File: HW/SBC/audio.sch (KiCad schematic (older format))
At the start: 13 parts, among them U13 LM386, U14 AY-3-8912

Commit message: Connected most hierarchical labels between the sheets. Added a connector to AY IO port.
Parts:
- added J6: AY-IO, Connect:IDC_Header_Straight_14pins, symbol CONN_02X07
- C16, C18, C19, C20: footprint (none) -> Capacitors_ThroughHole:C_Disc_D3.8mm_W2.6mm_P2.50mm
- C21: footprint (none) -> Capacitors_ThroughHole:CP_Radial_D6.3mm_P2.50mm
- LS1: footprint (none) -> Connect:PJ311_3.5mm_Jack
- R1, R2, R3, R4, R5: footprint (none) -> Resistors_ThroughHole:R_Axial_DIN0411_L9.9mm_D3.6mm_P12.70mm_Horizontal
- U13: footprint (none) -> Housings_DIP:DIP-8_W7.62mm_Socket
- U14: footprint (none) -> Housings_DIP:DIP-28_W15.24mm_Socket
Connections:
- net GND: now also J6.1 (P1), J6.2 (P2)
- net IO_A0: now also J6.5 (P5)
- net IO_A1: now also J6.6 (P6)
- net IO_A2: now also J6.7 (P7)
- net IO_A3: now also J6.8 (P8)
- net IO_A4: now also J6.9 (P9)
- net IO_A5: now also J6.10 (P10)
- net IO_A6: now also J6.11 (P11)
- net IO_A7: now also J6.12 (P12)
- net VCC: now also U14.19 (BC2), J6.13 (P13), J6.14 (P14)
- net CLK: now reaches U14.15 (CLK)
- net ~RES: now reaches U14.16 (~RESET)
- net V2CA1: now reaches U14.18 (BDir)
- net V2CA2: now reaches U14.20 (BC1)
- no-connect marks 4 -> 7
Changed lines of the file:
@@
 F 0 "U14" H 4775 4375 60  0000 C CNN
 F 1 "AY-3-8912" V 4975 3675 60  0000 C CNN
-F 2 "" H 4850 3900 60  0001 C CNN
+F 2 "Housings_DIP:DIP-28_W15.24mm_Socket" H 4850 3900 60  0001 C CNN
 F 3 "" H 4850 3900 60  0001 C CNN
 	1    4950 3675
@@
 F 0 "U13" H 3400 1875 50  0000 L CNN
 F 1 "LM386" H 3400 1775 50  0000 L CNN
-F 2 "" H 3450 1675 50  0001 C CNN
+F 2 "Housings_DIP:DIP-8_W7.62mm_Socket" H 3450 1675 50  0001 C CNN
 F 3 "" H 3550 1775 50  0001 C CNN
 	1    3350 1575
@@
 F 0 "LS1" H 4925 1800 50  0000 R CNN
 F 1 "Speaker" H 4925 1725 50  0000 R CNN
-F 2 "" H 4875 1375 50  0001 C CNN
+F 2 "Connect:PJ311_3.5mm_Jack" H 4875 1375 50  0001 C CNN
 F 3 "" H 4865 1525 50  0001 C CNN
 	1    4875 1575
@@
 F 0 "C19" H 3025 3825 50  0000 L CNN
 F 1 "10nF" H 2675 3825 50  0000 L CNN
-F 2 "" H 2950 3825 50  0001 C CNN
+F 2 "Capacitors_ThroughHole:C_Disc_D3.8mm_W2.6mm_P2.50mm" H 2950 3825 50  0001 C CNN
 F 3 "" H 2950 3825 50  0001 C CNN
 	1    2950 3825
@@
 F 0 "C16" V 2900 3450 50  0000 L CNN
 F 1 "2.2nF" V 2575 3425 50  0000 L CNN
-F 2 "" H 2750 3475 50  0001 C CNN
+F 2 "Capacitors_ThroughHole:C_Disc_D3.8mm_W2.6mm_P2.50mm" H 2750 3475 50  0001 C CNN
 F 3 "" H 2750 3475 50  0001 C CNN
 	1    2750 3475
@@
 F 0 "C18" V 2675 1075 50  0000 L CNN
 F 1 "10uF" V 2925 1025 50  0000 L CNN
-F 2 "" H 2800 1125 50  0001 C CNN
+F 2 "Capacitors_ThroughHole:C_Disc_D3.8mm_W2.6mm_P2.50mm" H 2800 1125 50  0001 C CNN
 F 3 "" H 2800 1125 50  0001 C CNN
 	1    2800 1125
@@
 U 1 1 59307F57
 P 3900 1775
-F 0 "C20" H 3910 1845 50  0000 L CNN
+F 0 "C20" H 3725 1700 50  0000 L CNN
 F 1 "47nF" H 3910 1695 50  0000 L CNN
-F 2 "" H 3900 1775 50  0001 C CNN
+F 2 "Capacitors_ThroughHole:C_Disc_D3.8mm_W2.6mm_P2.50mm" H 3900 1775 50  0001 C CNN
 F 3 "" H 3900 1775 50  0001 C CNN
 	1    3900 1775
@@
 F 0 "R3" V 3575 3450 50  0000 L CNN
 F 1 "4.7k" V 3400 3450 50  0000 L CNN
-F 2 "" H 3500 3475 50  0001 C CNN
+F 2 "Resistors_ThroughHole:R_Axial_DIN0411_L9.9mm_D3.6mm_P12.70mm_Horizontal" H 3500 3475 50  0001 C CNN
 F 3 "" H 3500 3475 50  0001 C CNN
 	1    3500 3475
@@
 F 0 "R4" H 3755 3845 50  0000 L CNN
 F 1 "1k" H 3755 3785 50  0000 L CNN
-F 2 "" H 3725 3825 50  0001 C CNN
+F 2 "Resistors_ThroughHole:R_Axial_DIN0411_L9.9mm_D3.6mm_P12.70mm_Horizontal" H 3725 3825 50  0001 C CNN
 F 3 "" H 3725 3825 50  0001 C CNN
 	1    3725 3825
@@
 F 0 "R5" V 3825 2025 50  0000 L CNN
 F 1 "10" V 3975 2025 50  0000 L CNN
-F 2 "" H 3900 2075 50  0001 C CNN
+F 2 "Resistors_ThroughHole:R_Axial_DIN0411_L9.9mm_D3.6mm_P12.70mm_Horizontal" H 3900 2075 50  0001 C CNN
 F 3 "" H 3900 2075 50  0001 C CNN
 	1    3900 2075
@@
 F 0 "R2" H 3275 3850 50  0000 L CNN
 F 1 "470" H 3275 3775 50  0000 L CNN
-F 2 "" H 3225 3825 50  0001 C CNN
+F 2 "Resistors_ThroughHole:R_Axial_DIN0411_L9.9mm_D3.6mm_P12.70mm_Horizontal" H 3225 3825 50  0001 C CNN
 F 3 "" H 3225 3825 50  0001 C CNN
 	1    3225 3825
@@
 F 0 "R1" V 2625 1650 50  0000 L CNN
 F 1 "22k" V 2775 1625 50  0000 L CNN
-F 2 "" H 2700 1675 50  0001 C CNN
+F 2 "Resistors_ThroughHole:R_Axial_DIN0411_L9.9mm_D3.6mm_P12.70mm_Horizontal" H 2700 1675 50  0001 C CNN
 F 3 "" H 2700 1675 50  0001 C CNN
 	1    2700 1675
@@
 F 0 "C21" V 4400 1525 50  0000 L CNN
 F 1 "220uF 10V" V 4150 1400 50  0000 L CNN
-F 2 "" H 4275 1575 50  0001 C CNN
+F 2 "Capacitors_ThroughHole:CP_Radial_D6.3mm_P2.50mm" H 4275 1575 50  0001 C CNN
 F 3 "" H 4275 1575 50  0001 C CNN
 	1    4275 1575
@@
 NoConn ~ 3350 1275
 $Comp
-L GND #PWR47
+L GND #PWR044
 U 1 1 59309AB4
 P 3250 2500
-F 0 "#PWR47" H 3250 2250 50  0001 C CNN
+F 0 "#PWR044" H 3250 2250 50  0001 C CNN
 F 1 "GND" H 3250 2350 50  0000 C CNN
 F 2 "" H 3250 2500 50  0001 C CNN
@@
 $EndComp
 $Comp
-L GND #PWR45
+L GND #PWR045
 U 1 1 5930A8FE
 P 2525 1125
-F 0 "#PWR45" H 2525 875 50  0001 C CNN
+F 0 "#PWR045" H 2525 875 50  0001 C CNN
 F 1 "GND" H 2525 975 50  0000 C CNN
 F 2 "" H 2525 1125 50  0001 C CNN
@@
 $EndComp
 $Comp
-L GND #PWR44
+L GND #PWR046
 U 1 1 5930AC61
 P 2300 4100
-F 0 "#PWR44" H 2300 3850 50  0001 C CNN
+F 0 "#PWR046" H 2300 3850 50  0001 C CNN
 F 1 "GND" H 2300 3950 50  0000 C CNN
 F 2 "" H 2300 4100 50  0001 C CNN
@@
 NoConn ~ 4450 3075
 $Comp
-L VCC #PWR48
+L VCC #PWR047
 U 1 1 5930B1EC
 P 4950 2725
-F 0 "#PWR48" H 4950 2575 50  0001 C CNN
+F 0 "#PWR047" H 4950 2575 50  0001 C CNN
 F 1 "VCC" H 4950 2875 50  0000 C CNN
 F 2 "" H 4950 2725 50  0001 C CNN
@@
 $EndComp
 $Comp
-L VCC #PWR46
+L VCC #PWR048
 U 1 1 5930B242
 P 3250 1075
-F 0 "#PWR46" H 3250 925 50  0001 C CNN
+F 0 "#PWR048" H 3250 925 50  0001 C CNN
 F 1 "VCC" H 3250 1225 50  0000 C CNN
 F 2 "" H 3250 1075 50  0001 C CNN
@@
 $EndComp
 $Comp
-L GND #PWR49
+L GND #PWR049
 U 1 1 5930BB05
 P 4950 4750
-F 0 "#PWR49" H 4950 4500 50  0001 C CNN
+F 0 "#PWR049" H 4950 4500 50  0001 C CNN
 F 1 "GND" H 4950 4600 50  0000 C CNN
 F 2 "" H 4950 4750 50  0001 C CNN
@@
 	5450 3775 5725 3775
 Wire Bus Line
-	5825 3675 5825 2800
+	5825 2800 5825 3675
 Wire Bus Line
 	5825 2800 6450 2800
@@
 	4025 3775 4025 4625
 Wire Bus Line
-	4025 4625 3550 4625
+	4025 4625 3350 4625
 Text Label 3550 4625 0    60   ~ 0
 IO_A[0..7]
-Text HLabel 3550 4625 0    60   BiDi ~ 0
-IO_A[0..7]
+Wire Wire Line
+	5450 3875 5900 3875
+Wire Wire Line
+	5450 4075 5900 4075
+$Comp
+L VCC #PWR050
+U 1 1 5933EB38
+P 5450 3975
+F 0 "#PWR050" H 5450 3825 50  0001 C CNN
+F 1 "VCC" H 5450 4125 50  0000 C CNN
+F 2 "" H 5450 3975 50  0001 C CNN
+F 3 "" H 5450 3975 50  0001 C CNN
+	1    5450 3975
+	0    1    1    0
+$EndComp
+Text HLabel 5900 3875 2    60   Input ~ 0
+V2CA2
+Text HLabel 5900 4075 2    60   Input ~ 0
+V2CA1
+NoConn ~ 5450 4175
+Wire Wire Line
+	5450 4275 5900 4275
+Wire Wire Line
+	5450 4375 5900 4375
+Text HLabel 5900 4275 2    60   Input ~ 0
+~RES
+Text HLabel 5900 4375 2    60   Input ~ 0
+CLK
+$Comp
+L VCC #PWR051
+U 1 1 593F1705
+P 1800 5800
+F 0 "#PWR051" H 1800 5650 50  0001 C CNN
+F 1 "VCC" H 1800 5950 50  0000 C CNN
+F 2 "" H 1800 5800 50  0001 C CNN
+F 3 "" H 1800 5800 50  0001 C CNN
+	1    1800 5800
+	1    0    0    -1
+$EndComp
+$Comp
+L GND #PWR052
+U 1 1 593F170B
+P 1800 4900
+F 0 "#PWR052" H 1800 4650 50  0001 C CNN
+F 1 "GND" H 1800 4750 50  0000 C CNN
+F 2 "" H 1800 4900 50  0001 C CNN
+F 3 "" H 1800 4900 50  0001 C CNN
+	1    1800 4900
+	1    0    0    -1
+$EndComp
+Wire Wire Line
+	1975 5300 2015 5230
+Wire Wire Line
+	1975 5400 2015 5330
+Wire Wire Line
+	1975 5500 2015 5430
+Wire Wire Line
+	1975 5600 2015 5530
+Wire Wire Line
+	2015 5230 2475 5230
+Wire Wire Line
+	2015 5330 2475 5330
+Wire Wire Line
+	2015 5430 2475 5430
+Wire Wire Line
+	2015 5530 2475 5530
+Wire Wire Line
+	2475 5230 3350 5050
+Wire Wire Line
+	2475 5330 3350 5300
+Wire Wire Line
+	2475 5430 3350 5550
+Wire Wire Line
+	2475 5530 3350 5800
+Wire Wire Line
+	3350 5175 2475 5300
+Wire Wire Line
+	3350 5425 2475 5400
+Wire Wire Line
+	3350 5675 2475 5500
+Wire Wire Line
+	3350 5925 2475 5600
+Wire Wire Line
+	2475 5800 2475 5700
+Wire Wire Line
+	1800 5800 2475 5800
+Wire Wire Line
+	1975 5800 1975 5700
+Wire Wire Line
+	2475 4900 2475 5100
+Wire Wire Line
+	1800 4900 2475 4900
+Wire Wire Line
+	1975 4900 1975 5100
+Connection ~ 1975 5800
+Connection ~ 1975 4900
+Text Label 3350 5050 2    60   ~ 0
+IO_A0
+Text Label 3350 5175 2    60   ~ 0
+IO_A1
+Text Label 3350 5300 2    60   ~ 0
+IO_A2
+Text Label 3350 5425 2    60   ~ 0
+IO_A3
+Text Label 3350 5550 2    60   ~ 0
+IO_A4
+Text Label 3350 5675 2    60   ~ 0
+IO_A5
+Text Label 3350 5800 2    60   ~ 0
+IO_A6
+Text Label 3350 5925 2    60   ~ 0
+IO_A7
+$Comp
+L CONN_02X07 J6
+U 1 1 593F16FE
+P 2225 5400
+F 0 "J6" H 2225 5800 50  0000 C CNN
+F 1 "AY-IO" V 2225 5400 50  0000 C CNN
+F 2 "Connect:IDC_Header_Straight_14pins" H 2225 4200 50  0001 C CNN
+F 3 "" H 2225 4200 50  0001 C CNN
+	1    2225 5400
+	1    0    0    -1
+$EndComp
+NoConn ~ 2475 5200
+NoConn ~ 1975 5200
+Wire Bus Line
+	3350 4625 3350 5925
 $EndSCHEMATC

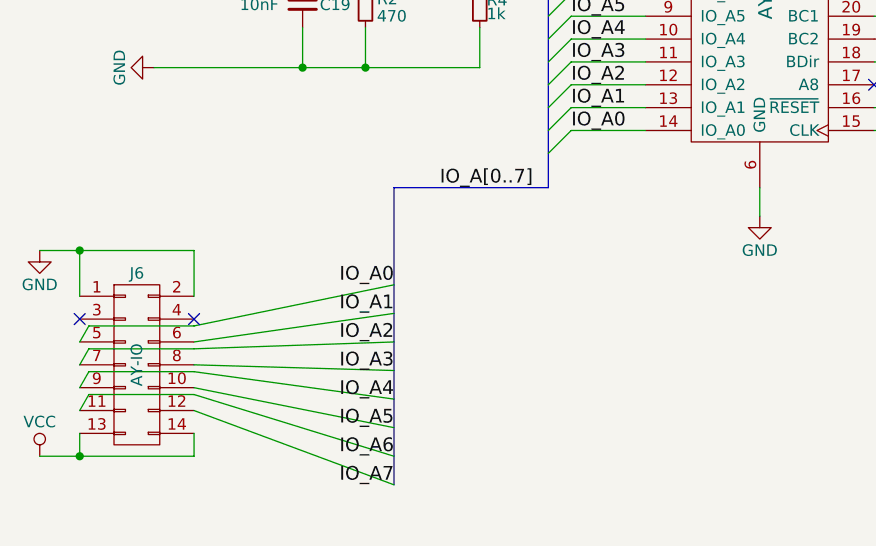
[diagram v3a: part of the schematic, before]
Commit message: Still no VCC net in PCBnew.
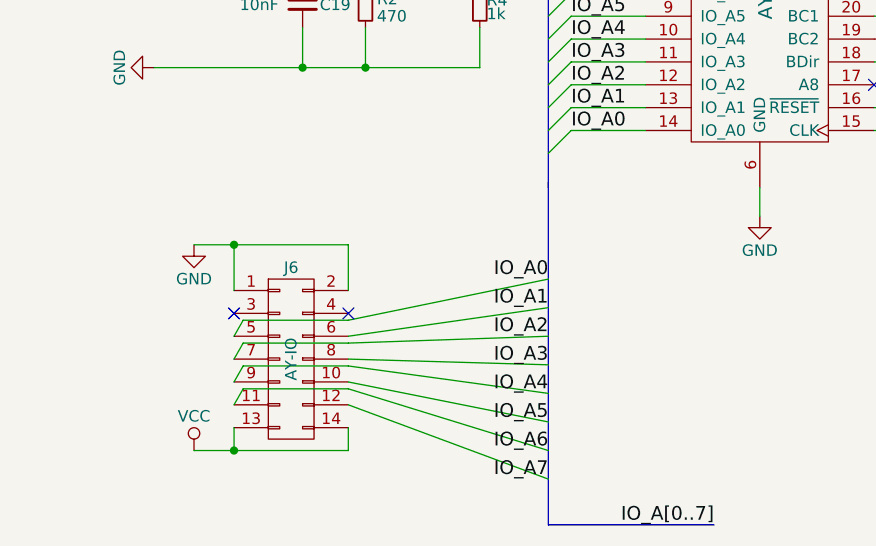
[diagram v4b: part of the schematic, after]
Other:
- moved on the sheet: J6
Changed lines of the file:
@@
 EESchema Schematic File Version 2
-LIBS:pluto-rescue
 LIBS:power
 LIBS:device
@@
 LIBS:pluto
 LIBS:pluto-cache
-LIBS:IDE_interface-cache
 EELAYER 25 0
 EELAYER END
@@
 NoConn ~ 3350 1275
 $Comp
-L GND #PWR044
+L GND #PWR042
 U 1 1 59309AB4
 P 3250 2500
-F 0 "#PWR044" H 3250 2250 50  0001 C CNN
+F 0 "#PWR042" H 3250 2250 50  0001 C CNN
 F 1 "GND" H 3250 2350 50  0000 C CNN
 F 2 "" H 3250 2500 50  0001 C CNN
@@
 $EndComp
 $Comp
-L GND #PWR045
+L GND #PWR043
 U 1 1 5930A8FE
 P 2525 1125
-F 0 "#PWR045" H 2525 875 50  0001 C CNN
+F 0 "#PWR043" H 2525 875 50  0001 C CNN
 F 1 "GND" H 2525 975 50  0000 C CNN
 F 2 "" H 2525 1125 50  0001 C CNN
@@
 $EndComp
 $Comp
-L GND #PWR046
+L GND #PWR044
 U 1 1 5930AC61
 P 2300 4100
-F 0 "#PWR046" H 2300 3850 50  0001 C CNN
+F 0 "#PWR044" H 2300 3850 50  0001 C CNN
 F 1 "GND" H 2300 3950 50  0000 C CNN
 F 2 "" H 2300 4100 50  0001 C CNN
@@
 NoConn ~ 4450 3075
 $Comp
-L VCC #PWR047
+L VCC #PWR045
 U 1 1 5930B1EC
 P 4950 2725
-F 0 "#PWR047" H 4950 2575 50  0001 C CNN
+F 0 "#PWR045" H 4950 2575 50  0001 C CNN
 F 1 "VCC" H 4950 2875 50  0000 C CNN
 F 2 "" H 4950 2725 50  0001 C CNN
@@
 $EndComp
 $Comp
-L VCC #PWR048
+L VCC #PWR046
 U 1 1 5930B242
 P 3250 1075
-F 0 "#PWR048" H 3250 925 50  0001 C CNN
+F 0 "#PWR046" H 3250 925 50  0001 C CNN
 F 1 "VCC" H 3250 1225 50  0000 C CNN
 F 2 "" H 3250 1075 50  0001 C CNN
@@
 $EndComp
 $Comp
-L GND #PWR049
+L GND #PWR047
 U 1 1 5930BB05
 P 4950 4750
-F 0 "#PWR049" H 4950 4500 50  0001 C CNN
+F 0 "#PWR047" H 4950 4500 50  0001 C CNN
 F 1 "GND" H 4950 4600 50  0000 C CNN
 F 2 "" H 4950 4750 50  0001 C CNN
@@
 Wire Bus Line
 	4025 3775 4025 4625
-Wire Bus Line
-	4025 4625 3350 4625
-Text Label 3550 4625 0    60   ~ 0
+Text Label 4750 6100 2    60   ~ 0
 IO_A[0..7]
 Wire Wire Line
@@
 	5450 4075 5900 4075
 $Comp
-L VCC #PWR050
+L VCC #PWR048
 U 1 1 5933EB38
 P 5450 3975
-F 0 "#PWR050" H 5450 3825 50  0001 C CNN
+F 0 "#PWR048" H 5450 3825 50  0001 C CNN
 F 1 "VCC" H 5450 4125 50  0000 C CNN
 F 2 "" H 5450 3975 50  0001 C CNN
@@
 CLK
 $Comp
-L VCC #PWR051
+L VCC #PWR049
 U 1 1 593F1705
-P 1800 5800
-F 0 "#PWR051" H 1800 5650 50  0001 C CNN
-F 1 "VCC" H 1800 5950 50  0000 C CNN
-F 2 "" H 1800 5800 50  0001 C CNN
-F 3 "" H 1800 5800 50  0001 C CNN
-	1    1800 5800
-	1    0    0    -1
-$EndComp
-$Comp
-L GND #PWR052
+P 2475 5775
+F 0 "#PWR049" H 2475 5625 50  0001 C CNN
+F 1 "VCC" H 2475 5925 50  0000 C CNN
+F 2 "" H 2475 5775 50  0001 C CNN
+F 3 "" H 2475 5775 50  0001 C CNN
+	1    2475 5775
+	1    0    0    -1
+$EndComp
+$Comp
+L GND #PWR050
 U 1 1 593F170B
-P 1800 4900
-F 0 "#PWR052" H 1800 4650 50  0001 C CNN
-F 1 "GND" H 1800 4750 50  0000 C CNN
-F 2 "" H 1800 4900 50  0001 C CNN
-F 3 "" H 1800 4900 50  0001 C CNN
-	1    1800 4900
-	1    0    0    -1
-$EndComp
-Wire Wire Line
-	1975 5300 2015 5230
-Wire Wire Line
-	1975 5400 2015 5330
-Wire Wire Line
-	1975 5500 2015 5430
-Wire Wire Line
-	1975 5600 2015 5530
-Wire Wire Line
-	2015 5230 2475 5230
-Wire Wire Line
-	2015 5330 2475 5330
-Wire Wire Line
-	2015 5430 2475 5430
-Wire Wire Line
-	2015 5530 2475 5530
-Wire Wire Line
-	2475 5230 3350 5050
-Wire Wire Line
-	2475 5330 3350 5300
-Wire Wire Line
-	2475 5430 3350 5550
-Wire Wire Line
-	2475 5530 3350 5800
-Wire Wire Line
-	3350 5175 2475 5300
-Wire Wire Line
-	3350 5425 2475 5400
-Wire Wire Line
-	3350 5675 2475 5500
-Wire Wire Line
-	3350 5925 2475 5600
-Wire Wire Line
-	2475 5800 2475 5700
-Wire Wire Line
-	1800 5800 2475 5800
-Wire Wire Line
-	1975 5800 1975 5700
-Wire Wire Line
-	2475 4900 2475 5100
-Wire Wire Line
-	1800 4900 2475 4900
-Wire Wire Line
-	1975 4900 1975 5100
-Connection ~ 1975 5800
-Connection ~ 1975 4900
-Text Label 3350 5050 2    60   ~ 0
+P 2475 4875
+F 0 "#PWR050" H 2475 4625 50  0001 C CNN
+F 1 "GND" H 2475 4725 50  0000 C CNN
+F 2 "" H 2475 4875 50  0001 C CNN
+F 3 "" H 2475 4875 50  0001 C CNN
+	1    2475 4875
+	1    0    0    -1
+$EndComp
+Wire Wire Line
+	2650 5275 2690 5205
+Wire Wire Line
+	2650 5375 2690 5305
+Wire Wire Line
+	2650 5475 2690 5405
+Wire Wire Line
+	2650 5575 2690 5505
+Wire Wire Line
+	2690 5205 3150 5205
+Wire Wire Line
+	2690 5305 3150 5305
+Wire Wire Line
+	2690 5405 3150 5405
+Wire Wire Line
+	2690 5505 3150 5505
+Wire Wire Line
+	3150 5205 4025 5025
+Wire Wire Line
+	3150 5305 4025 5275
+Wire Wire Line
+	3150 5405 4025 5525
+Wire Wire Line
+	3150 5505 4025 5775
+Wire Wire Line
+	4025 5150 3150 5275
+Wire Wire Line
+	4025 5400 3150 5375
+Wire Wire Line
+	4025 5650 3150 5475
+Wire Wire Line
+	4025 5900 3150 5575
+Wire Wire Line
+	3150 5775 3150 5675
+Wire Wire Line
+	2475 5775 3150 5775
+Wire Wire Line
+	2650 5775 2650 5675
+Wire Wire Line
+	3150 4875 3150 5075
+Wire Wire Line
+	2475 4875 3150 4875
+Wire Wire Line
+	2650 4875 2650 5075
+Connection ~ 2650 5775
+Connection ~ 2650 4875
+Text Label 4025 5025 2    60   ~ 0
 IO_A0
-Text Label 3350 5175 2    60   ~ 0
+Text Label 4025 5150 2    60   ~ 0
 IO_A1
-Text Label 3350 5300 2    60   ~ 0
+Text Label 4025 5275 2    60   ~ 0
 IO_A2
-Text Label 3350 5425 2    60   ~ 0
+Text Label 4025 5400 2    60   ~ 0
 IO_A3
-Text Label 3350 5550 2    60   ~ 0
+Text Label 4025 5525 2    60   ~ 0
 IO_A4
-Text Label 3350 5675 2    60   ~ 0
+Text Label 4025 5650 2    60   ~ 0
 IO_A5
-Text Label 3350 5800 2    60   ~ 0
+Text Label 4025 5775 2    60   ~ 0
 IO_A6
-Text Label 3350 5925 2    60   ~ 0
+Text Label 4025 5900 2    60   ~ 0
 IO_A7
 $Comp
 L CONN_02X07 J6
 U 1 1 593F16FE
-P 2225 5400
-F 0 "J6" H 2225 5800 50  0000 C CNN
-F 1 "AY-IO" V 2225 5400 50  0000 C CNN
-F 2 "Connect:IDC_Header_Straight_14pins" H 2225 4200 50  0001 C CNN
-F 3 "" H 2225 4200 50  0001 C CNN
-	1    2225 5400
-	1    0    0    -1
-$EndComp
-NoConn ~ 2475 5200
-NoConn ~ 1975 5200
+P 2900 5375
+F 0 "J6" H 2900 5775 50  0000 C CNN
+F 1 "AY-IO" V 2900 5375 50  0000 C CNN
+F 2 "Connect:IDC_Header_Straight_14pins" H 2900 4175 50  0001 C CNN
+F 3 "" H 2900 4175 50  0001 C CNN
+	1    2900 5375
+	1    0    0    -1
+$EndComp
+NoConn ~ 3150 5175
+NoConn ~ 2650 5175
 Wire Bus Line
-	3350 4625 3350 5925
+	4025 4600 4025 6100
+Wire Bus Line
+	4025 6100 4750 6100
 $EndSCHEMATC

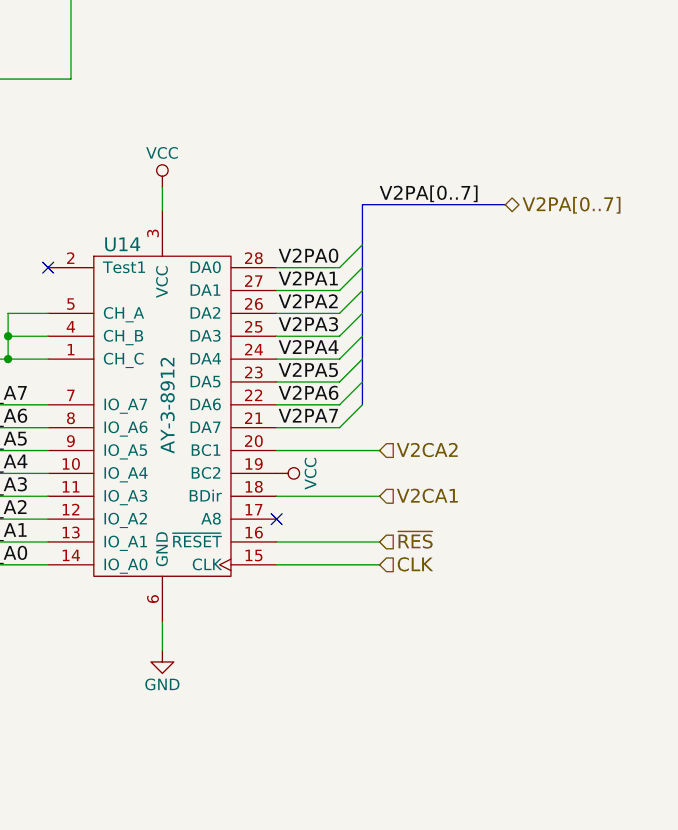
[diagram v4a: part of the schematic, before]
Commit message: New PCB layout. Added datasheet for AY-3-8912 and LM386.
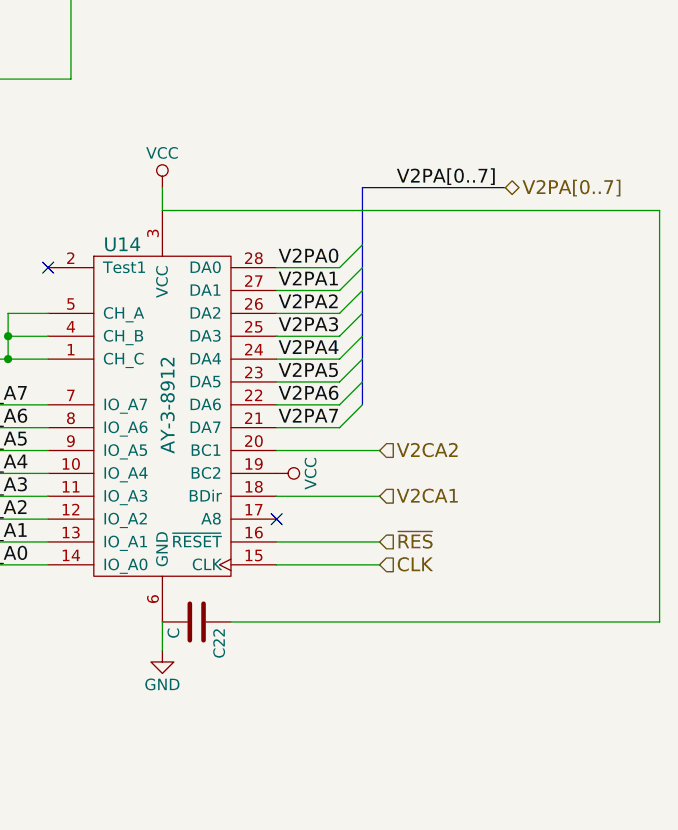
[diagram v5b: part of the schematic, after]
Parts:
- added C22: C, Capacitors_ThroughHole:C_Disc_D3.8mm_W2.6mm_P2.50mm, symbol C
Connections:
- net GND: now also C22.2
- net VCC: now also C22.1
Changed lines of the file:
@@
 	5450 3775 5725 3775
 Wire Bus Line
-	5825 2800 5825 3675
-Wire Bus Line
-	5825 2800 6450 2800
-Text Label 5900 2800 0    60   ~ 0
+	5825 2725 5825 3675
+Wire Bus Line
+	5825 2725 6450 2725
+Text Label 5975 2725 0    60   ~ 0
 V2PA[0..7]
-Text HLabel 6450 2800 2    60   BiDi ~ 0
+Text HLabel 6450 2725 2    60   BiDi ~ 0
 V2PA[0..7]
 Wire Wire Line
@@
 Wire Bus Line
 	4025 6100 4750 6100
+$Comp
+L C C22
+U 1 1 593A070B
+P 5100 4625
+F 0 "C22" H 5125 4725 50  0000 L CNN
+F 1 "C" H 5125 4525 50  0000 L CNN
+F 2 "Capacitors_ThroughHole:C_Disc_D3.8mm_W2.6mm_P2.50mm" H 5138 4475 50  0001 C CNN
+F 3 "" H 5100 4625 50  0001 C CNN
+	1    5100 4625
+	0    1    1    0
+$EndComp
+Wire Wire Line
+	5250 4625 7125 4625
+Wire Wire Line
+	7125 4625 7125 2825
+Wire Wire Line
+	7125 2825 4950 2825
 $EndSCHEMATC
